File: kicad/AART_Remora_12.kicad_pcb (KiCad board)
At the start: 4 copper layers, 16.2 x 23.2 mm, 82 parts, among them J1 Conn_01x01_Pin, J10 Conn_01x01_Pin, J11 Conn_01x01_Pin, J2 Conn_01x01_Pin, J3 Conn_01x01_Pin, J4 Conn_01x04, J5 Conn_01x01, J6 Conn_01x01, J7 Conn_01x01, J8 Conn_01x01_Pin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

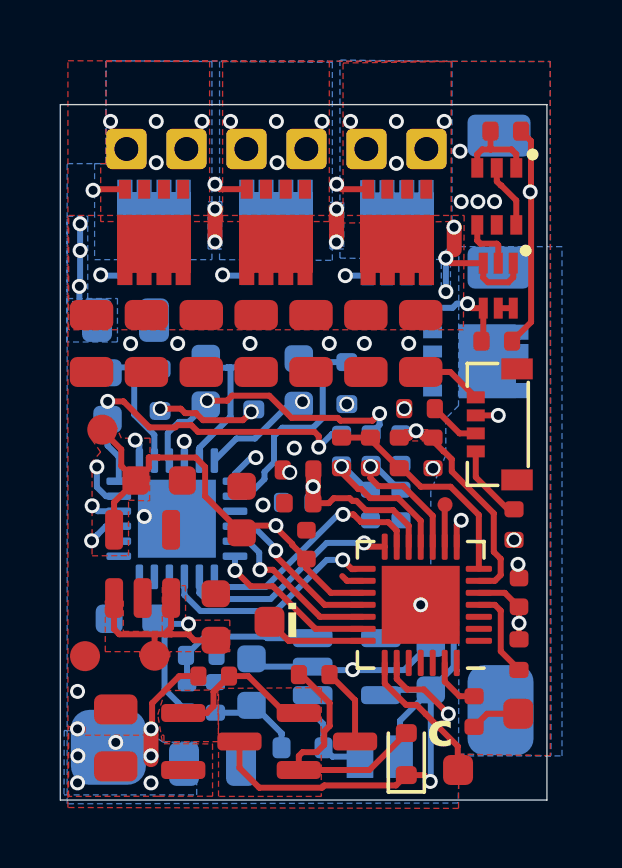
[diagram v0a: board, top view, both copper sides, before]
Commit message: Updated foot prints and 3d
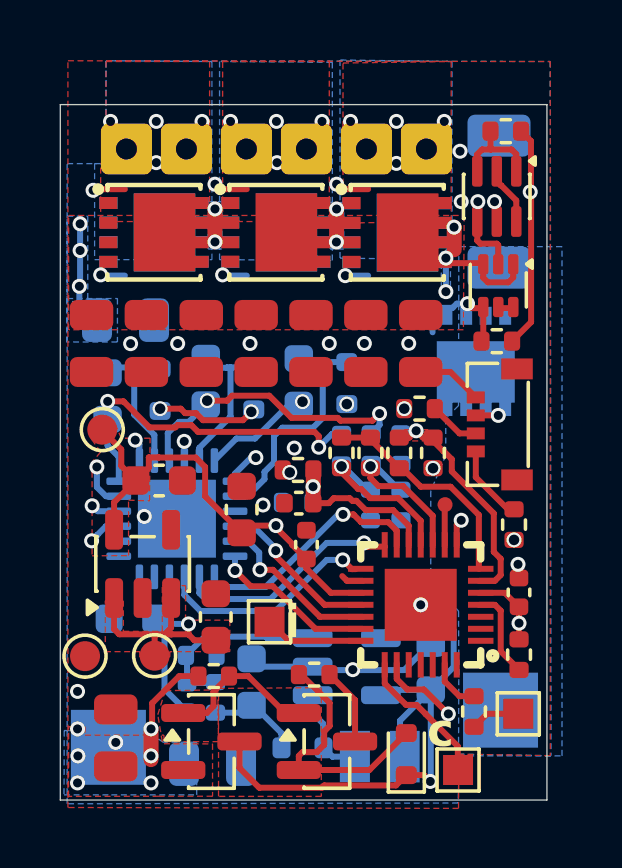
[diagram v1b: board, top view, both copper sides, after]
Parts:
- C11, C12, C13: footprint Capacitor_SMD:C_0805_2012Metric -> AART12Footprints:C_0805_2012Metric_22µF
- C14, C15, C16, C17, C18, C19, C20: footprint AART11footprints:C_0805_2012Metric_22µF -> AART12Footprints:C_0805_2012Metric_22µF
- J4: footprint AART11footprints:HDG 1x04 P0.6 Horizontal -> AART12Footprints:HDG 1x04 P0.6 Horizontal
- L1: footprint AART11footprints:L_Sunltech_SLW2010P -> AART12Footprints:IND-SMD_L2.0-W1.6
- Q10, Q4, Q5, Q6, Q7, Q8, Q9: footprint Package_SON:VSON-8_3.3x3.3mm_P0.65mm_NexFET -> AART12Footprints:DFN-8_L3.2-W3.1-P0.65-LS3.4-BL
- U4: footprint Package_DFN_QFN:QFN-28-1EP_4x4mm_P0.4mm_EP2.6x2.6mm -> AART12Footprints:QFN-28_L4.0-W4.0-P0.40-TL-EP2.4
